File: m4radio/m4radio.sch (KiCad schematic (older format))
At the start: 97 parts, among them IC1 NCP4620, IC10 Si4463, IC2 MCP2562, IC3 STM32F405RxTx, IC4 MAX-M8Q, IC5 NC7SZ04, IC6 NCP380, IC7 CS2100-CP, IC8 SL18860DC, IC9 SN74LVC1G0832, J1 WEST TOP, J2 EAST TOP, P1 SWD_TC, P2 COAX, P3 COAX, Y1 TCXO

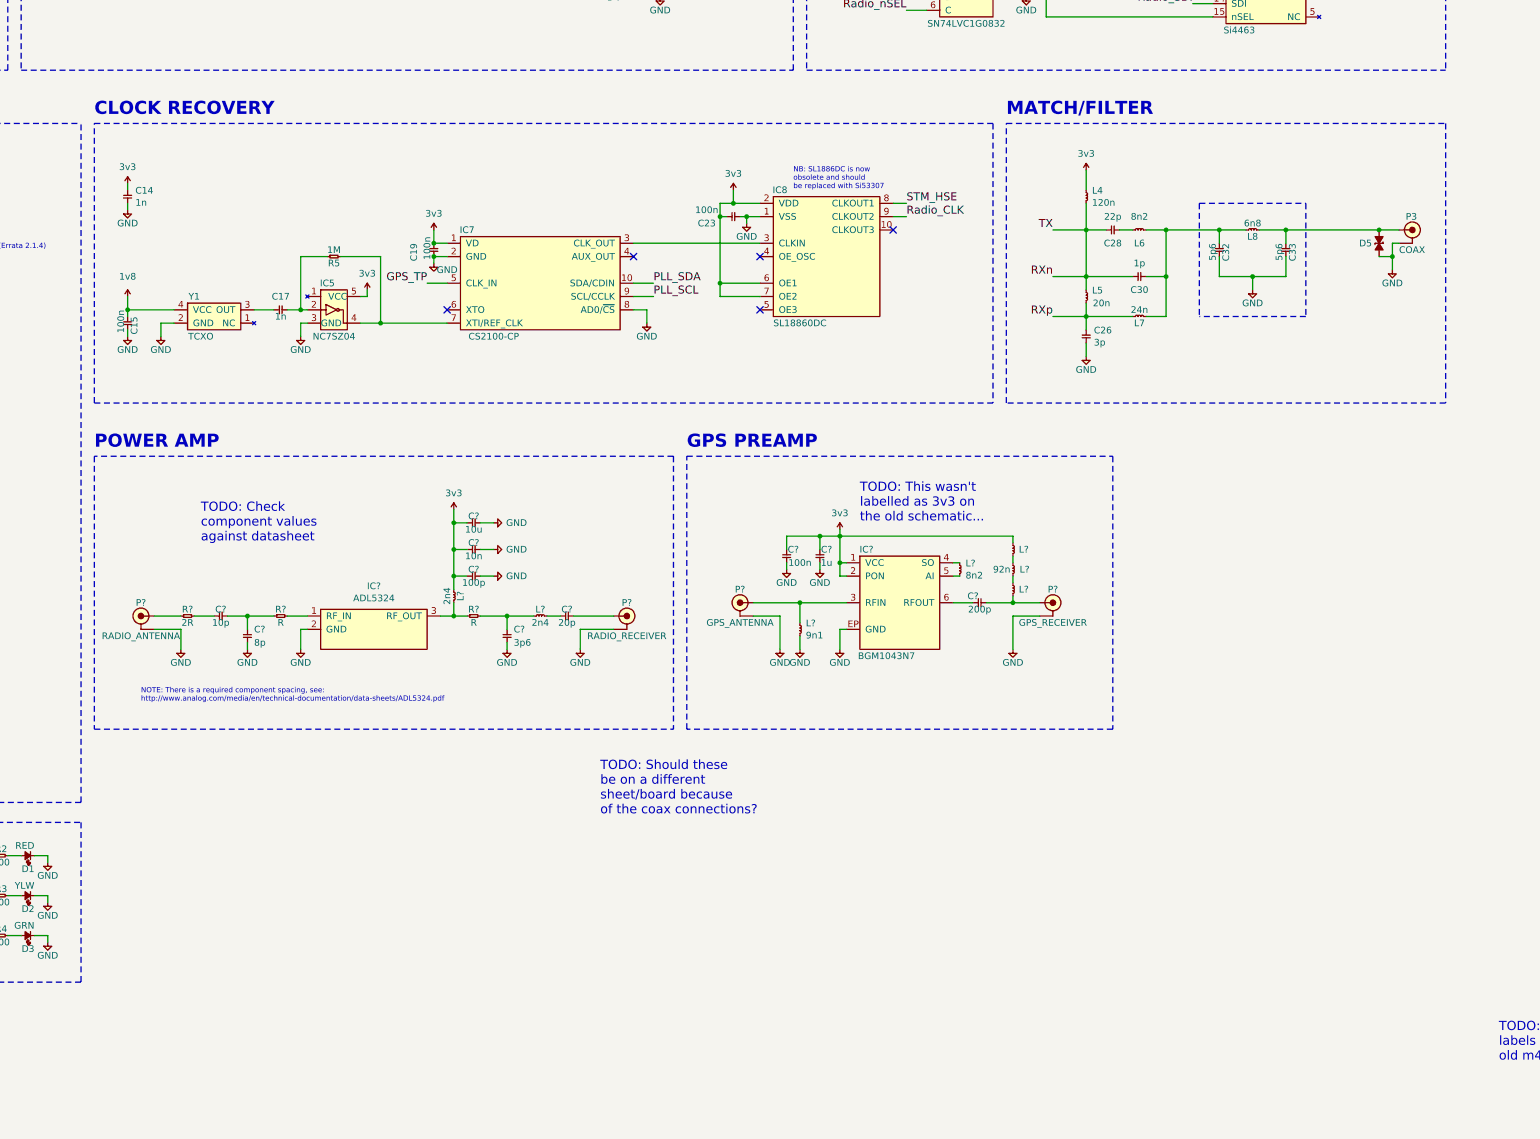
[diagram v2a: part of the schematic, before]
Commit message: Change clock buffer to Si53307
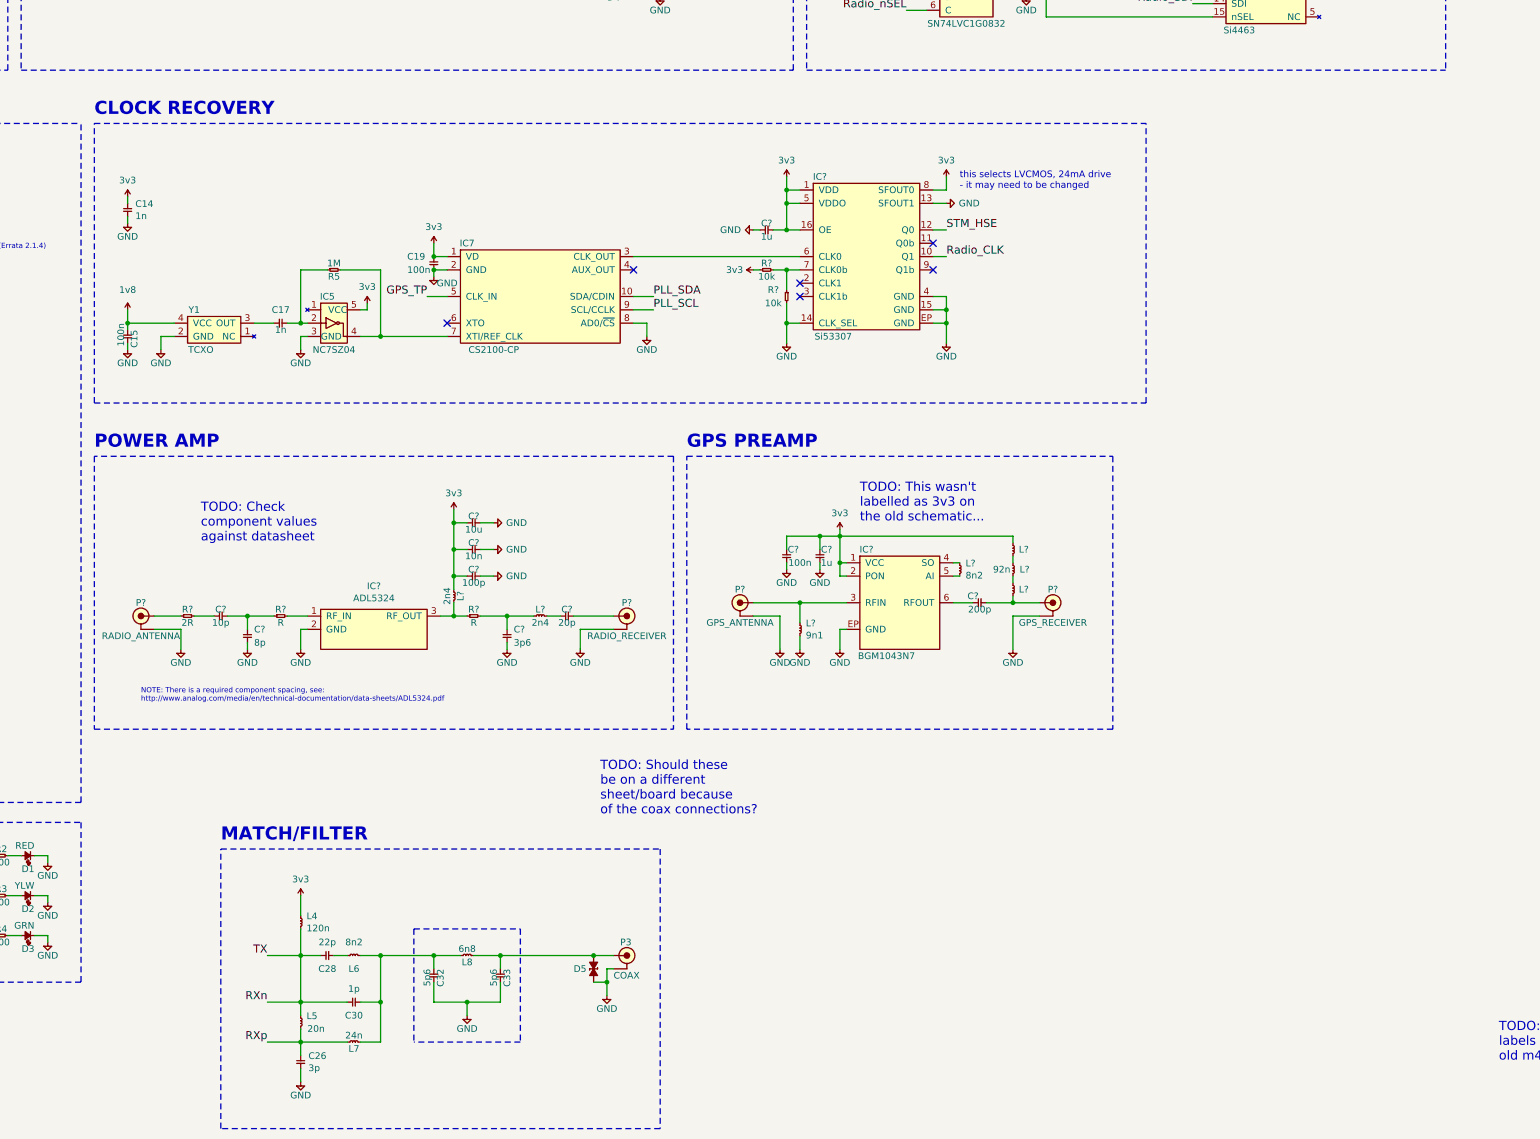
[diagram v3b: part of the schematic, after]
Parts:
- removed C23: 100n, symbol cusf-kicad:C
- removed IC8: SL18860DC, agg:DFN-10-SL18860DC, symbol cusf-kicad:SL18860DC
- added C?: 1u, symbol cusf-kicad:C
- added IC?: Si53307, agg:DFN-10-SL18860DC, symbol cusf-kicad:Si53307
- added R? (x2): 10k, symbol cusf-kicad:R
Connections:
- net 3v3: now also C?.2, IC?.1 (VDD), IC?.16 (OE), IC?.5 (VDDO), IC?.8 (SFOUT0), R?.1
- net GND: now also C?.1, IC?.13 (SFOUT1), IC?.14 (CLK_SEL), IC?.15 (GND), IC?.4 (GND), IC?.EP (GND), R?.2
- net Radio_CLK: now also IC?.10 (Q1)
- net STM_HSE: now also IC?.12 (Q0)
- net at IC7.3 (CLK_OUT): now also IC?.6 (CLK0)
- new net: IC?.7 (CLK0b), R?.1, R?.2
- no-connect marks 63 -> 64
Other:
- note added: "this selects LVCMOS, 24mA drive\n- it may need to be changed"
- note removed: "NB: SL1886DC is now\nobsolete and should\nbe replaced with Si53307"
- moved on the sheet: C14, C15, C17, C19, C26, C28, C30, C32, C33, D5, IC5, IC7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

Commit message: Reorganise radio
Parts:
- removed D4: ESD_DIODE, agg:0402, symbol cusf-kicad:ESD_DIODE
- removed P2, P3: COAX, agg:SMA-EDGE, symbol cusf-kicad:COAX
- removed P?: GPS_RECEIVER, agg:SMA-EDGE, symbol cusf-kicad:COAX
- removed P?: RADIO_RECEIVER, agg:SMA-EDGE, symbol cusf-kicad:COAX
- added D?: ESD_DIODE, agg:0402, symbol cusf-kicad:ESD_DIODE
- P?: value RADIO_ANTENNA -> TELEM_ANTENNA
- renumbered C2 to C?, C8 to C?, C9 to C?, C6 to C?, C3 to C?, C4 to C?, C10 to C?, C5 to C?, C7 to C?, C12 to C?, C11 to C?, C16 to C?, C15 to C?, C21 to C?, C17 to C?, C18 to C?, C19 to C?, C14 to C?, C20 to C?, C1 to C?, C13 to C?, C31 to C?, C29 to C?, C27 to C?, C25 to C?, C24 to C?, C22 to C?, C26 to C?, C30 to C?, C28 to C?, C32 to C?, C33 to C?, D1 to D?, D2 to D?, D3 to D?, D5 to D?, IC2 to IC?, IC3 to IC?, IC4 to IC?, IC5 to IC?, IC7 to IC?, IC6 to IC?, IC1 to IC?, IC9 to IC?, IC10 to IC?, J1 to J?, J2 to J?, L1 to L?, L2 to L?, L3 to L?, L5 to L?, L7 to L?, L6 to L?, L4 to L?, L8 to L?, P1 to P?, R1 to R?, R2 to R?, R3 to R?, R4 to R?, R5 to R?, R6 to R?, R7 to R?, R8 to R?, R9 to R?, Y1 to Y?
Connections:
- net 3v3: now also L?.2; no longer L?.1
- net GND: now also D?.1, D?.1; no longer D?.2
- net Radio_SDN: no longer IC?.1 (SDN)
- net GPS_ANT: now reaches C?.1, IC?.11 (RF_IN), L?.2
- net GPS_ANT: now also C?.2, L?.2
- net at IC?.3 (RF_OUT), R?.1: now also L?.1; no longer L?.2
- net at IC?.3 (RFIN), L?.1, P?.1 (RF): now also D?.2
- net at P?.1 (RF), R?.1: now also D?.2
- net at C?.2: now also C?.1, L?.2
- net Radio_CLK renamed RADIO_CLK
- net Radio_GATE renamed RADIO_GATE
- net Radio_GPIO1 renamed RADIO_GPIO1
- net Radio_SCLK renamed RADIO_SCLK
- net Radio_SDI renamed RADIO_SDI
- net Radio_SDO renamed RADIO_SDO
- net Radio_nIRQ renamed RADIO_nIRQ
- net Radio_nSEL renamed RADIO_nSEL
- net STM_HSE renamed MCU_CLK
- new net RADIO_SDN: IC?.1 (SDN)
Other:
- note added: "TELEMETRY POWER AMP"
- note added: "TELEMETRY RADIO"
- note added: "https://www.silabs.com/Support%20Documents/TechnicalDocs/AN627.pdf"
- note removed: "MATCH/FILTER"
- note removed: "POWER AMP"
- note removed: "RADIO"
- note removed: "TODO: Should these\nbe on a different\nsheet/board because\nof the coax connections?"
- note removed: "TODO: This wasn't\nlabelled as 3v3 on\nthe old schematic..."
- moved on the sheet: C?, D?, IC?, L?, P?, R?, Y?

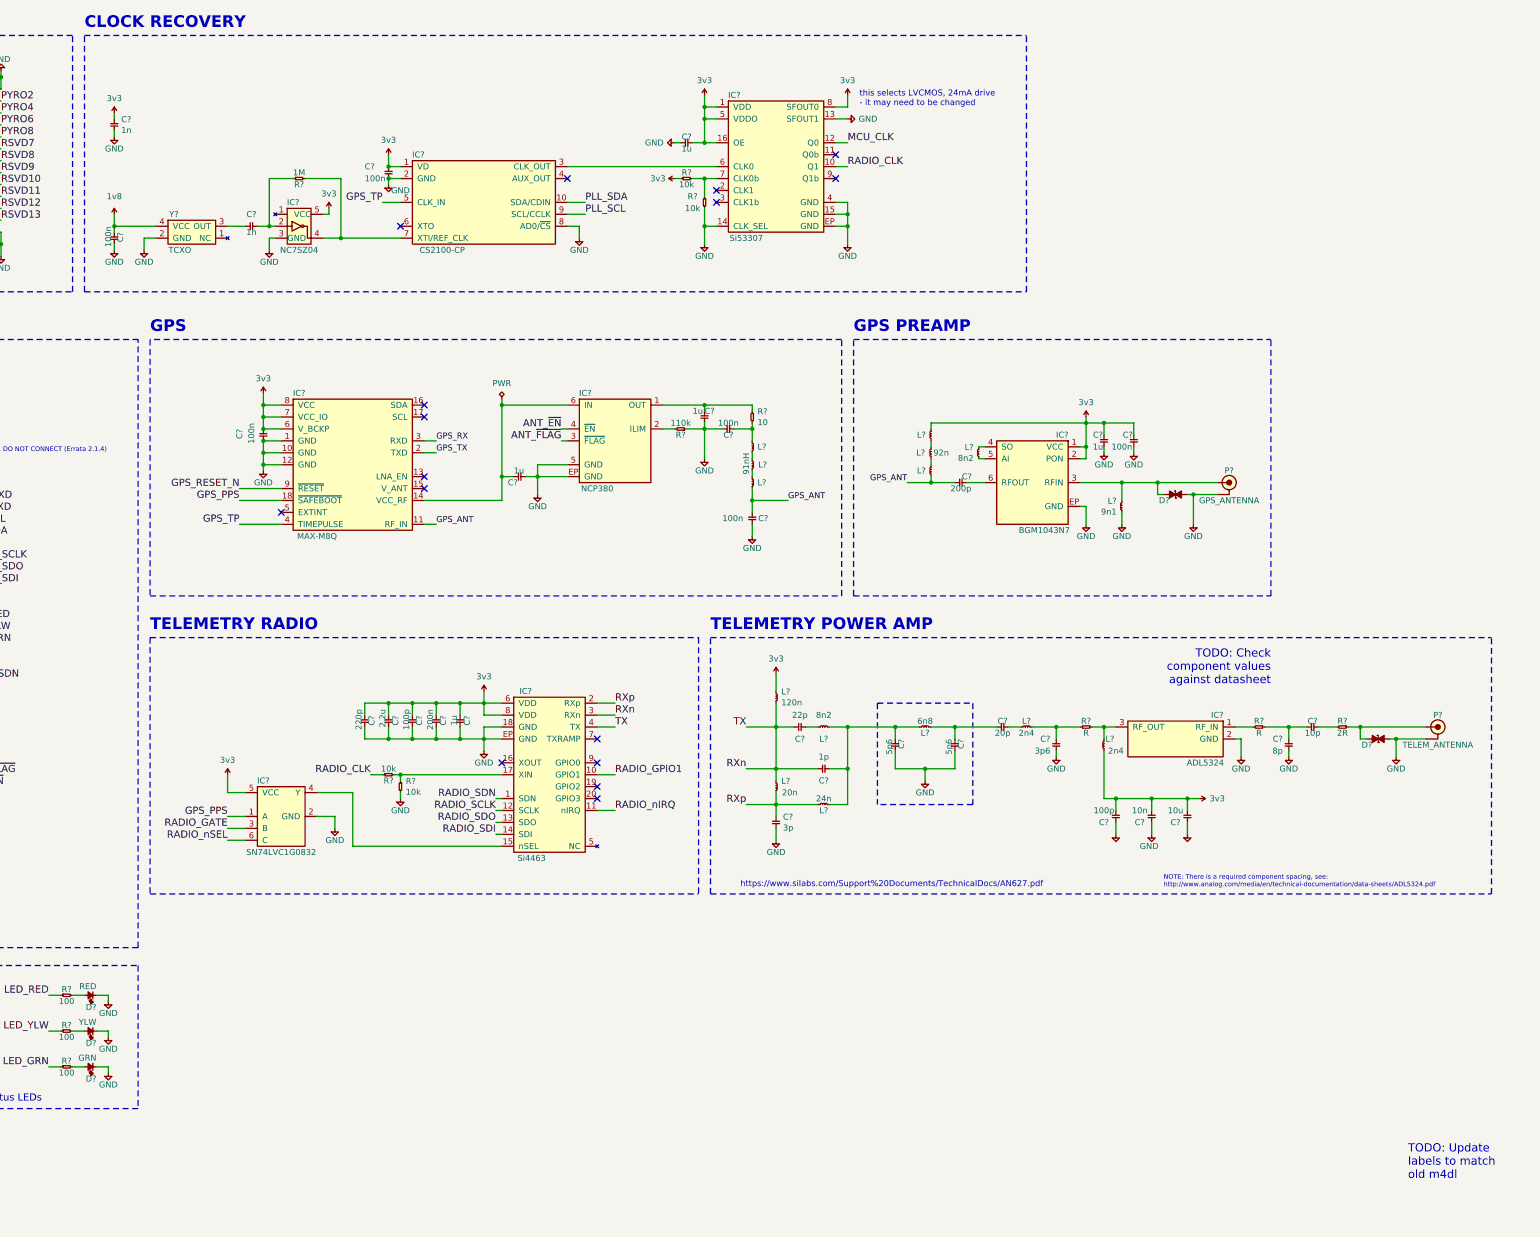
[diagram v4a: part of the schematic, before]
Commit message: Minor layout fixes
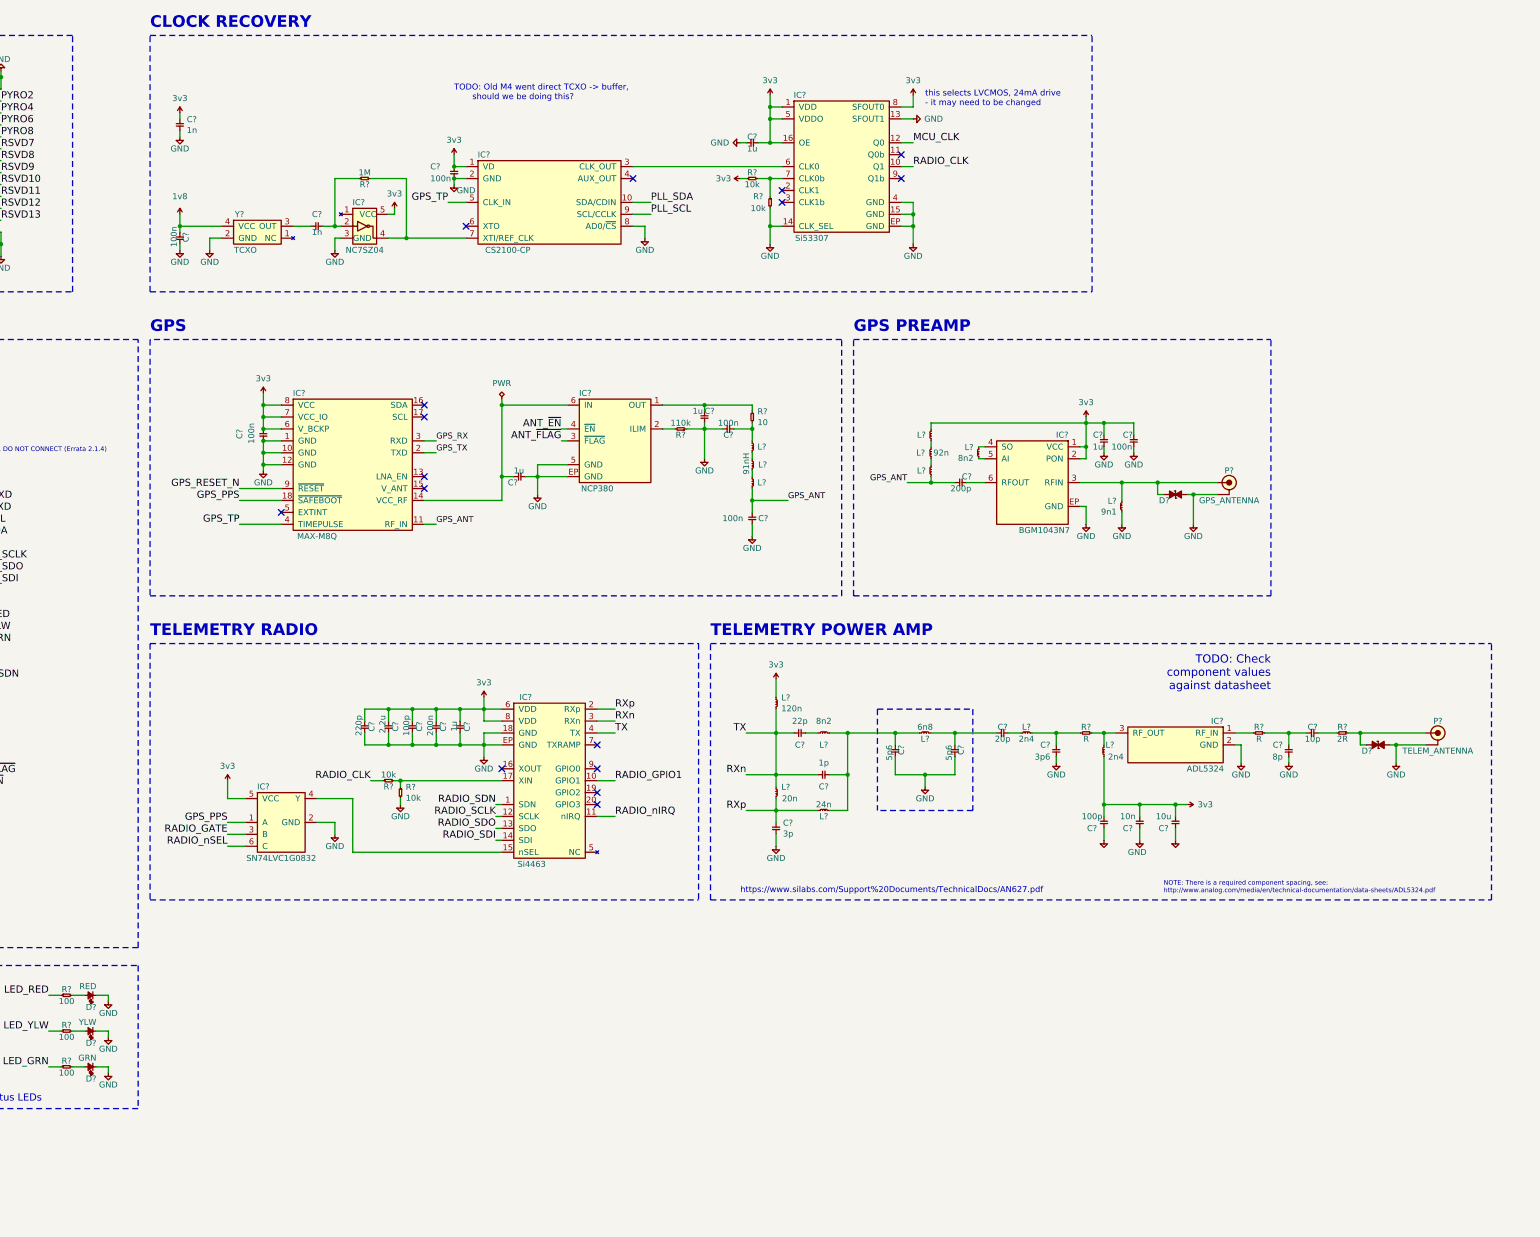
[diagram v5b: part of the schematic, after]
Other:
- note added: "TODO: Old M4 went direct TCXO -> buffer,\n should we be doing this?"
- note removed: "TODO: Update\nlabels to match\nold m4dl"
- moved on the sheet: C?, D?, IC?, L?, P?, R?, Y?
